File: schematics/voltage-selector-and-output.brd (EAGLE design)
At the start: 40.3 x 30.5 mm, 24 parts, among them IC2 ATTINY85, IC3 MCP41010P, IC4 5V, IC5 MIC2941, X1 USB-A-H

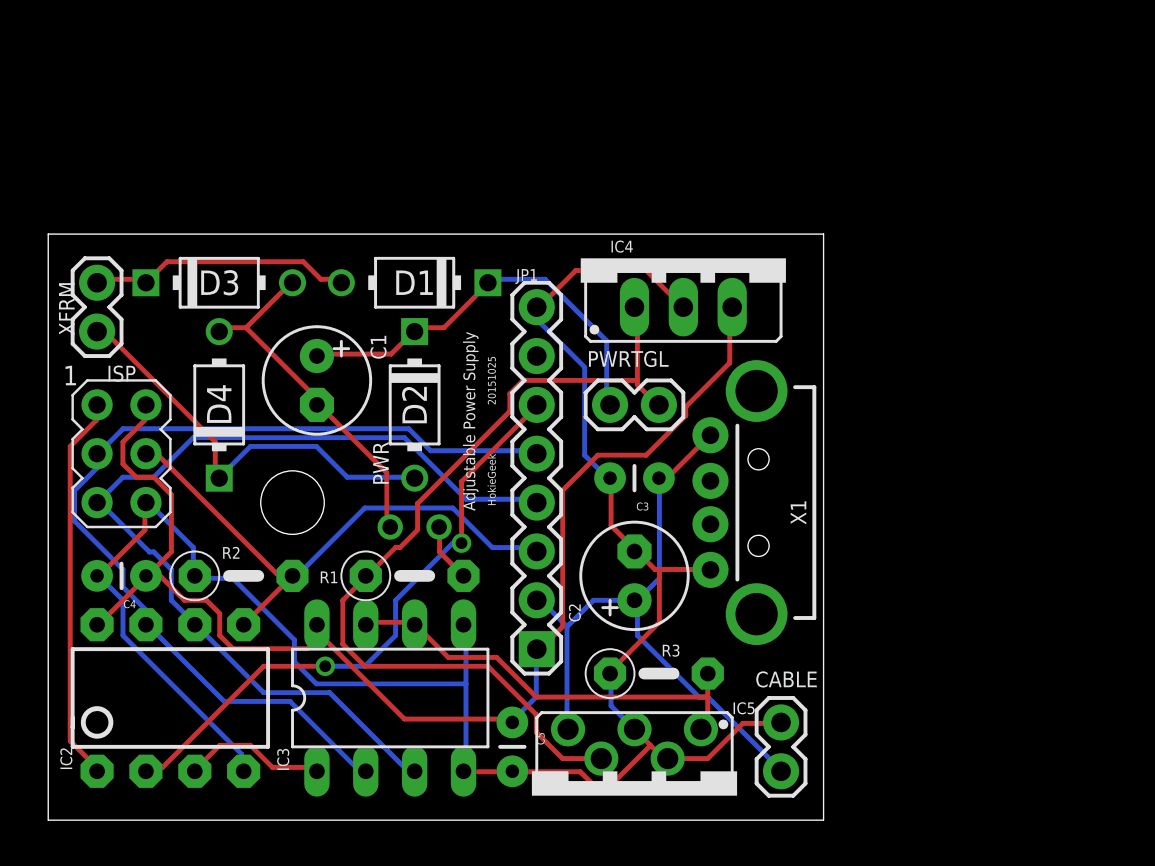
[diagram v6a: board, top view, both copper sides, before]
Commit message: Decided to give SMT another chance
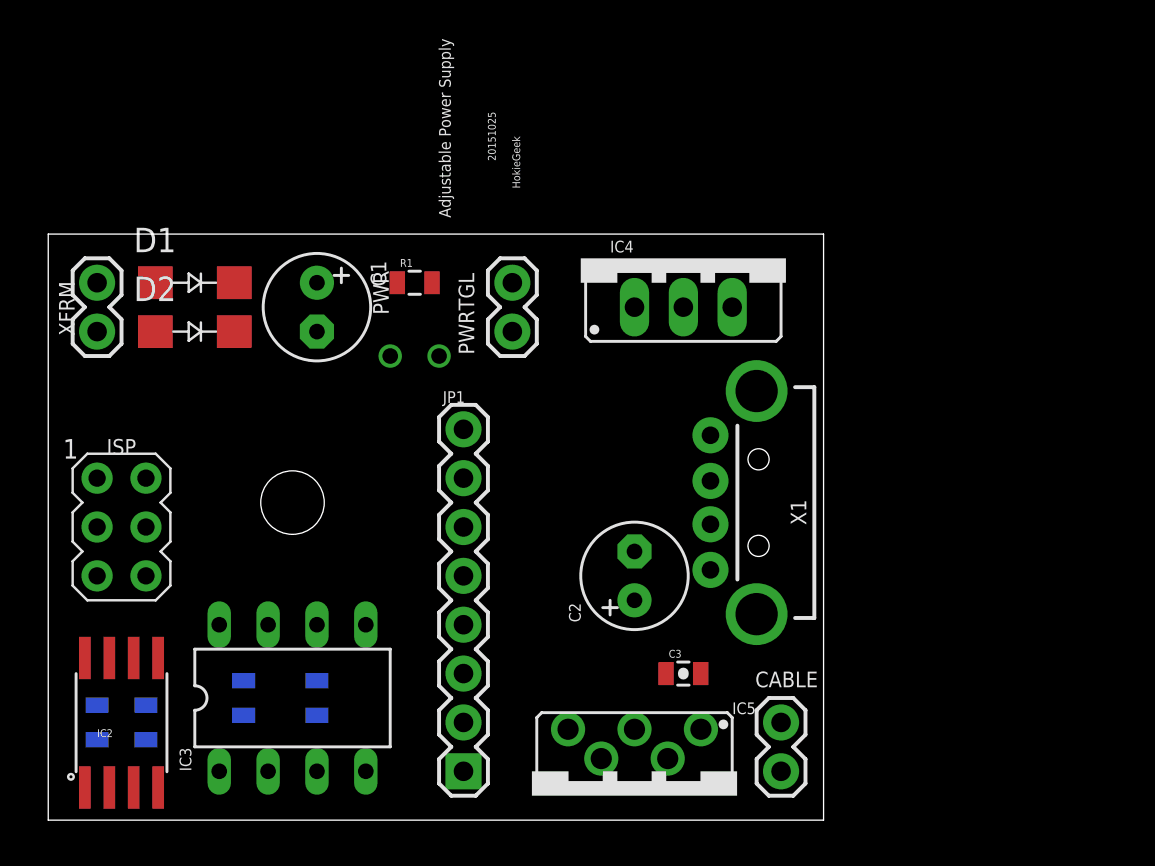
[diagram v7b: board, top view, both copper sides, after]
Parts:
- C3, C4, C5: device SparkFun-Capacitors:CAP-PTH-SMALL -> SparkFun-Capacitors:0805-CAP
- D1, D2, D3, D4: device gm-diodes:DO41-3 -> diode:SMA-DO214AC
- IC2: value ATTINY85 -> Tiny85-20-SMT; device SparkFun:DIP08 -> SparkFun-DigitalIC:SO08-EIAJ
- R1, R2: device rcl-ez:0207/5V -> SparkFun-Resistors:0805
- R3: value 1K -> 1k; device rcl-ez:0207/5V -> SparkFun-Resistors:0805
- moved R3 17.8 mm to (14.0, 6.35), flipped to the bottom, turned to 90 degrees
- moved R1 15.2 mm to (19.1, 27.9)
- moved C5 14.0 mm to (10.2, 6.35), flipped to the bottom
- moved D2 12.0 mm to (7.62, 25.4), turned to 0 degrees
- moved D1 11.4 mm to (7.62, 27.9), turned to 0 degrees
- moved C3 10.2 mm to (33.0, 7.62), turned to 0 degrees
- moved R2 9.16 mm to (5.08, 5.08), flipped to the bottom, turned to 90 degrees
- moved PWR 8.89 mm to (19.1, 24.1)
- moved C4 8.03 mm to (2.54, 5.08), flipped to the bottom, turned to 270 degrees
- moved JP1 7.41 mm to (21.6, 2.54)
- moved PWRTGL 6.35 mm to (24.1, 25.4), turned to 90 degrees
- moved IC3 5.08 mm to (12.7, 6.35)
- moved D4 4.02 mm to (7.62, 25.4), flipped to the bottom, turned to 0 degrees
- moved C1 3.81 mm to (14.0, 26.7)
- moved ISP 3.81 mm to (3.81, 15.2)
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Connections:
- removed net N$10: PWR.A, R1.2
- new net N$3: PWR.A, R1.1
- net GND: now also D4.K; no longer D4.C
- net N$2: now also D3.K; no longer D3.C
- net N$9: now also D1.K, D2.K; no longer D1.C, D2.C
- net VCC: now also R1.2; no longer R1.1
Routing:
- net AGND: track 106.1 -> 0.00 mm
- net VIC: track 68.0 -> 0.00 mm
- net PB2: track 49.5 -> 0.00 mm
- net PB1: track 49.0 -> 0.00 mm
- net VCC: track 45.8 -> 0.00 mm
- net VADJ: track 34.4 -> 0.00 mm
- net PB3: track 31.2 -> 0.00 mm, vias 2 -> 0
- net PB0: track 29.1 -> 0.00 mm
- net N$1: track 22.5 -> 0.00 mm
- net GND: track 22.3 -> 0.00 mm
- net N$9: track 21.6 -> 0.00 mm
- net PB5: track 20.2 -> 0.00 mm
- net N$5: track 18.7 -> 0.00 mm
- net N$2: track 13.8 -> 0.00 mm
- net PB4: track 7.58 -> 0.00 mm
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
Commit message: Smaller and smaller. Gotta save on them bucks!
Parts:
- added C6: 0.1uF, SparkFun-Capacitors:0805-CAP
- moved PWRTGL 13.1 mm to (12.7, 19.1)
- moved STANDOFF1 13.0 mm to (25.4, 14.0)
- moved C1 12.8 mm to (12.7, 14.0), turned to 0 degrees
- moved R1 10.5 mm to (16.5, 17.8), flipped to the bottom, turned to 270 degrees
- moved IC4 8.13 mm to (27.9, 22.9)
- moved D1 6.35 mm to (7.62, 21.6)
- moved D3 6.35 mm to (7.62, 21.6), turned to 0 degrees
- moved D2 6.35 mm to (7.62, 19.1)
- moved D4 6.35 mm to (7.62, 19.1)
- moved XFRM 6.35 mm to (2.54, 19.1)
- moved C2 4.58 mm to (27.9, 8.89)
- moved PWR 4.58 mm to (16.5, 20.3)
- moved X1 2.54 mm to (36.8, 14.0)
- moved CABLE 2.54 mm to (35.6, 2.54), turned to 0 degrees
- moved IC5 2.54 mm to (27.9, 1.27)
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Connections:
- net AGND: now also C6.2
- net VIC: now also C6.1
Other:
- board size 40.3 x 30.5 mm -> 40.3 x 24.1 mm
